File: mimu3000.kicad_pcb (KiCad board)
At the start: 2 copper layers, 54.4 x 26.2 mm, 14 parts, among them SW1 P_MISO, SW2 P_MOSI, U1 ATTINY13A-SSU, U2 H11F1M

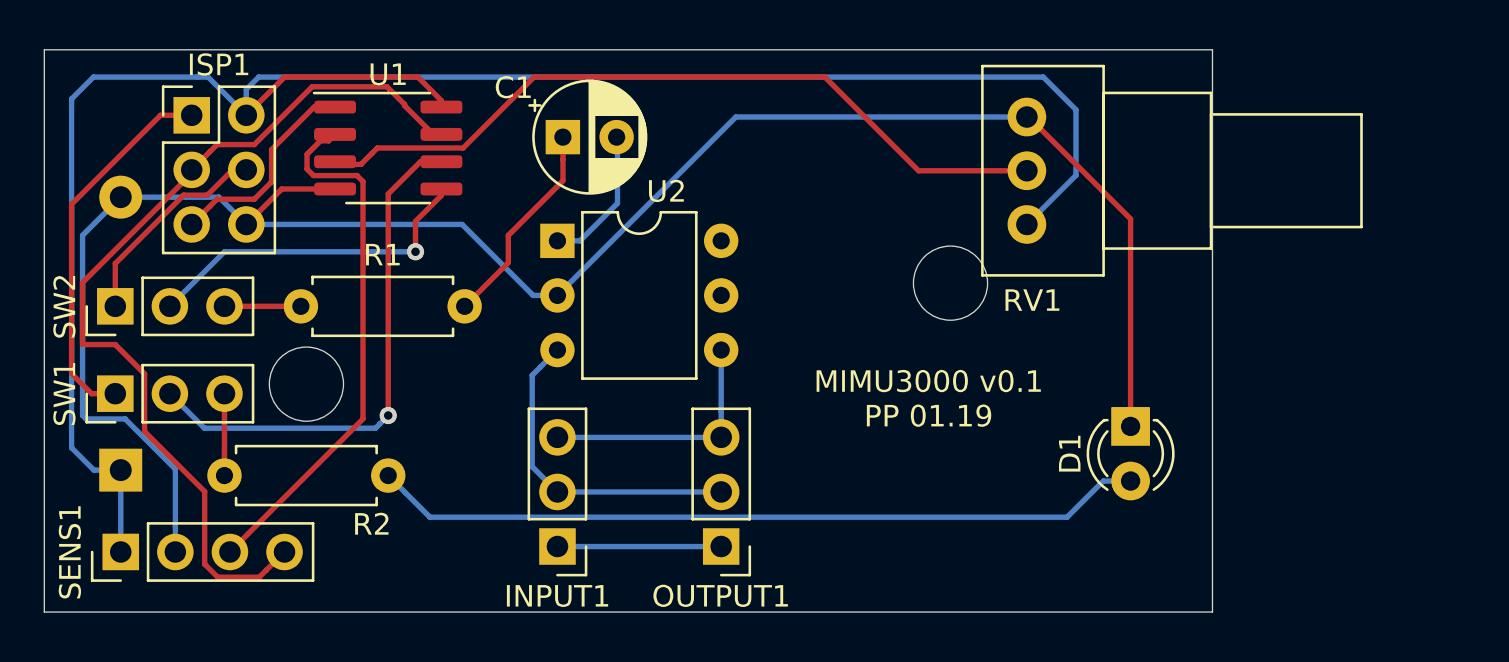
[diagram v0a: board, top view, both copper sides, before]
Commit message: Updated to using new low R_on optocoupler
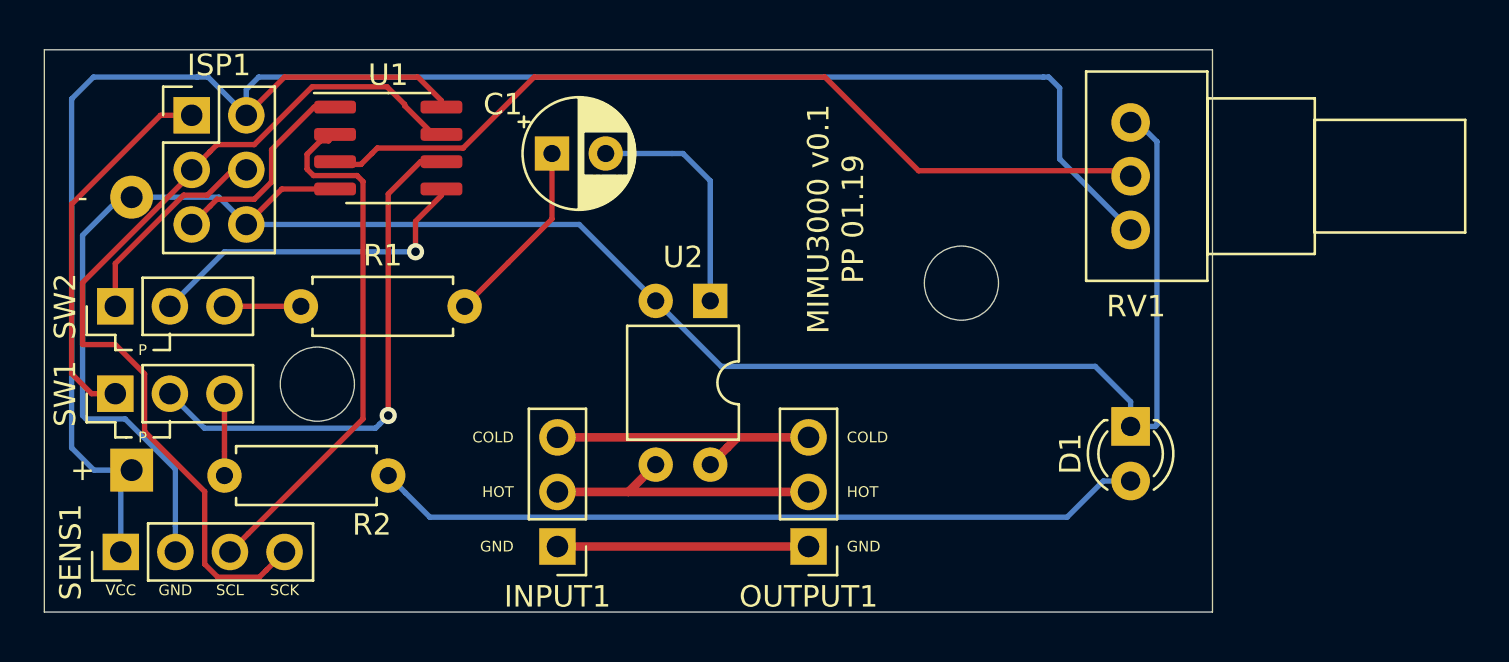
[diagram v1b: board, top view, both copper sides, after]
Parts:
- U2: value H11F1M -> AQY211EH; footprint Package_DIP:DIP-6_W7.62mm -> Package_DIP:DIP-4_W7.62mm
- moved U2 7.64 mm to (194.8, 112.3), turned to 270 degrees
- moved RV1 4.83 mm to (214.4, 109.0)
- moved OUTPUT1 4.06 mm to (199.4, 123.7)
- moved C1 0.92 mm to (187.5, 105.4)
- moved BT1 0.51 mm to (167.9, 120.1)
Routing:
- net Net-(RV1-Pad2): track 35.7 -> 40.7 mm
- net Net-(C1-Pad2): track 6.60 -> 11.0 mm
- net Net-(BT1-Pad2): track 88.9 -> 93.1 mm
- net Net-(INPUT1-Pad1): track 7.87 -> 11.7 mm
- net Net-(INPUT1-Pad3): track 11.7 -> 13.5 mm
- net Net-(INPUT1-Pad2): track 15.2 -> 13.5 mm
- net Net-(C1-Pad1): track 9.77 -> 8.80 mm
- net Net-(BT1-Pad1): track 89.6 -> 90.1 mm
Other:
- board text added: "+"
- board text added: "-"
- board text added: "COLD"
- board text added: "GND"
- board text added: "HOT"
- board text added: "P"
- board text added: "SCK"
- board text added: "SCL"
- board text added: "VCC"

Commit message: Fixed courtyard
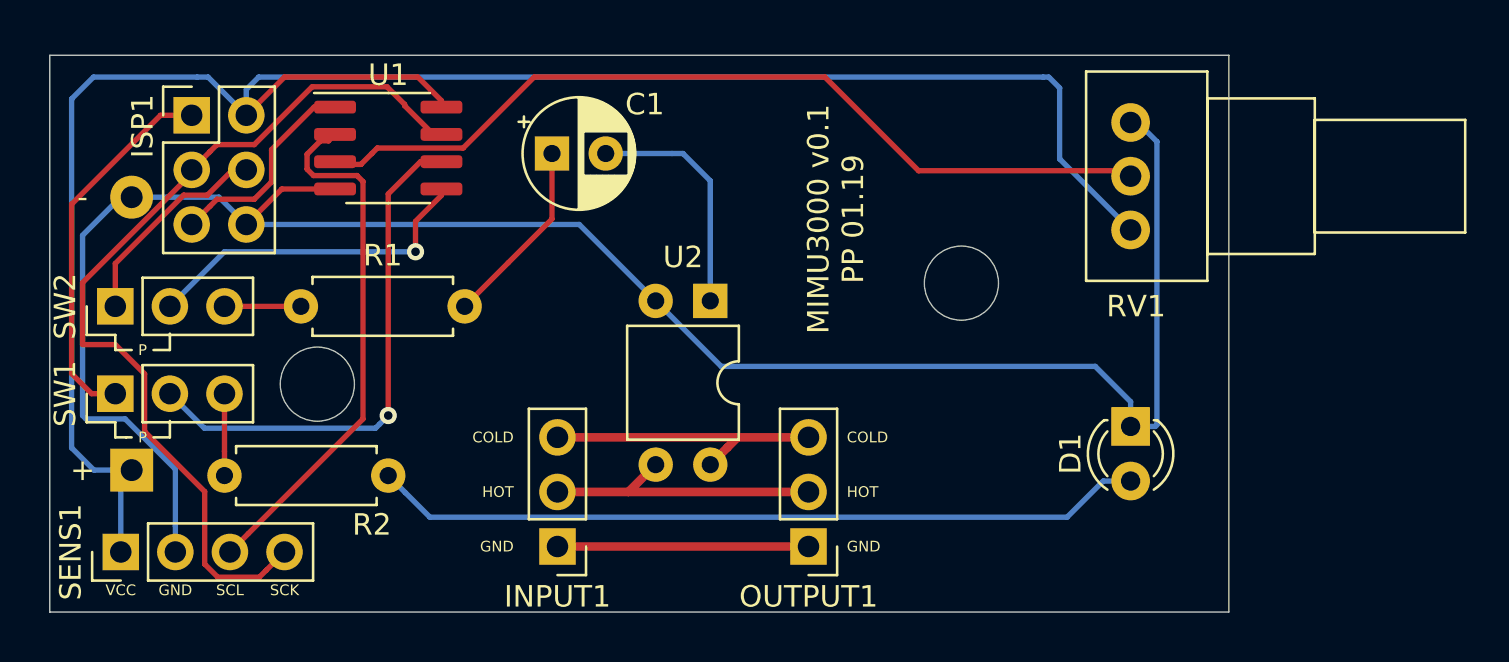
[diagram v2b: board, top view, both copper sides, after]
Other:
- board size 54.4 x 26.2 mm -> 54.9 x 25.9 mm
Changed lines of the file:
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@@
   (general
     (thickness 1.6)
-    (drawings 39)
+    (drawings 38)
     (tracks 138)
     (zones 0)
@@
     (descr "Through hole straight pin header, 2x03, 2.54mm pitch, double rows")
     (tags "Through hole pin header THT 2x03 2.54mm double row")
-    (fp_text reference ISP1 (at 1.27 -2.33) (layer F.SilkS)
+    (fp_text reference ISP1 (at -2.286 0.508 270) (layer F.SilkS)
       (effects (font (size 1 1) (thickness 0.15)))
     )
@@
     (descr "CP, Radial series, Radial, pin pitch=2.50mm, , diameter=5mm, Electrolytic Capacitor")
     (tags "CP Radial series Radial pin pitch 2.50mm  diameter 5mm Electrolytic Capacitor")
-    (fp_text reference C1 (at -2.286 -2.286) (layer F.SilkS)
+    (fp_text reference C1 (at 4.318 -2.286) (layer F.SilkS)
       (effects (font (size 1 1) (thickness 0.15)))
     )
@@
     )
   )
+  (gr_line (start 164.084 126.746) (end 164.084 100.838) (layer Edge.Cuts) (width 0.05))
+  (dimension 54.864 (width 0.15) (layer Dwgs.User)
+    (gr_text "54,864 mm" (at 191.516 138.099985) (layer Dwgs.User)
+      (effects (font (size 1 1) (thickness 0.15)))
+    )
+    (feature1 (pts (xy 218.948 126.746) (xy 218.948 137.386406)))
+    (feature2 (pts (xy 164.084 126.746) (xy 164.084 137.386406)))
+    (crossbar (pts (xy 164.084 136.799985) (xy 218.948 136.799985)))
+    (arrow1a (pts (xy 218.948 136.799985) (xy 217.821496 137.386406)))
+    (arrow1b (pts (xy 218.948 136.799985) (xy 217.821496 136.213564)))
+    (arrow2a (pts (xy 164.084 136.799985) (xy 165.210504 137.386406)))
+    (arrow2b (pts (xy 164.084 136.799985) (xy 165.210504 136.213564)))
+  )
   (gr_text GND (at 185.674 123.698) (layer F.SilkS)
     (effects (font (size 0.5 0.5) (thickness 0.1)) (justify right))
@@
   (gr_line (start 169.672 118.618) (end 169.672 117.856) (layer F.SilkS) (width 0.12))
   (gr_line (start 167.132 117.916) (end 167.132 118.618) (layer F.SilkS) (width 0.12))
-  (dimension 26.162 (width 0.15) (layer Dwgs.User)
-    (gr_text "26,162 mm" (at 159.99 113.665 90) (layer Dwgs.User)
-      (effects (font (size 1 1) (thickness 0.15)))
-    )
-    (feature1 (pts (xy 163.83 100.584) (xy 160.703579 100.584)))
-    (feature2 (pts (xy 163.83 126.746) (xy 160.703579 126.746)))
-    (crossbar (pts (xy 161.29 126.746) (xy 161.29 100.584)))
-    (arrow1a (pts (xy 161.29 100.584) (xy 161.876421 101.710504)))
-    (arrow1b (pts (xy 161.29 100.584) (xy 160.703579 101.710504)))
-    (arrow2a (pts (xy 161.29 126.746) (xy 161.876421 125.619496)))
-    (arrow2b (pts (xy 161.29 126.746) (xy 160.703579 125.619496)))
-  )
-  (dimension 54.356 (width 0.15) (layer Dwgs.User)
-    (gr_text "54,356 mm" (at 191.008 133.888) (layer Dwgs.User)
-      (effects (font (size 1 1) (thickness 0.15)))
-    )
-    (feature1 (pts (xy 218.186 126.746) (xy 218.186 133.174421)))
-    (feature2 (pts (xy 163.83 126.746) (xy 163.83 133.174421)))
-    (crossbar (pts (xy 163.83 132.588) (xy 218.186 132.588)))
-    (arrow1a (pts (xy 218.186 132.588) (xy 217.059496 133.174421)))
-    (arrow1b (pts (xy 218.186 132.588) (xy 217.059496 132.001579)))
-    (arrow2a (pts (xy 163.83 132.588) (xy 164.956504 133.174421)))
-    (arrow2b (pts (xy 163.83 132.588) (xy 164.956504 132.001579)))
+  (dimension 25.908 (width 0.15) (layer Dwgs.User)
+    (gr_text "25,908 mm" (at 160.244 113.792 90) (layer Dwgs.User)
+      (effects (font (size 1 1) (thickness 0.15)))
+    )
+    (feature1 (pts (xy 164.084 100.838) (xy 160.957579 100.838)))
+    (feature2 (pts (xy 164.084 126.746) (xy 160.957579 126.746)))
+    (crossbar (pts (xy 161.544 126.746) (xy 161.544 100.838)))
+    (arrow1a (pts (xy 161.544 100.838) (xy 162.130421 101.964504)))
+    (arrow1b (pts (xy 161.544 100.838) (xy 160.957579 101.964504)))
+    (arrow2a (pts (xy 161.544 126.746) (xy 162.130421 125.619496)))
+    (arrow2b (pts (xy 161.544 126.746) (xy 160.957579 125.619496)))
   )
   (gr_text "MIMU3000 v0.1\nPP 01.19" (at 200.66 108.458 90) (layer F.SilkS)
     (effects (font (size 1 1) (thickness 0.15)))
   )
-  (gr_line (start 163.83 100.584) (end 218.186 100.584) (layer Edge.Cuts) (width 0.05))
-  (gr_line (start 163.83 126.746) (end 163.83 100.584) (layer Edge.Cuts) (width 0.05))
-  (gr_line (start 218.186 126.746) (end 163.83 126.746) (layer Edge.Cuts) (width 0.05))
-  (gr_line (start 218.186 100.584) (end 218.186 126.746) (layer Edge.Cuts) (width 0.05))
-  (gr_line (start 163.83 126.746) (end 163.83 100.584) (layer B.CrtYd) (width 0.05))
-  (gr_line (start 218.186 126.746) (end 163.83 126.746) (layer B.CrtYd) (width 0.05))
-  (gr_line (start 218.186 100.584) (end 218.186 126.746) (layer B.CrtYd) (width 0.05))
-  (gr_line (start 163.83 100.584) (end 218.186 100.584) (layer B.CrtYd) (width 0.05))
-  (gr_line (start 218.186 100.584) (end 218.186 101.092) (layer F.CrtYd) (width 0.05))
-  (gr_line (start 163.83 100.584) (end 218.186 100.584) (layer F.CrtYd) (width 0.05))
-  (gr_line (start 163.83 126.746) (end 163.83 100.584) (layer F.CrtYd) (width 0.05))
-  (gr_line (start 218.186 126.746) (end 163.83 126.746) (layer F.CrtYd) (width 0.05))
-  (gr_line (start 218.186 101.092) (end 218.186 126.746) (layer F.CrtYd) (width 0.05))
+  (gr_line (start 164.084 100.838) (end 218.948 100.838) (layer Edge.Cuts) (width 0.05))
+  (gr_line (start 218.948 126.746) (end 164.084 126.746) (layer Edge.Cuts) (width 0.05))
+  (gr_line (start 218.948 100.838) (end 218.948 126.746) (layer Edge.Cuts) (width 0.05))
+  (gr_line (start 164.084 126.746) (end 164.084 100.838) (layer B.CrtYd) (width 0.05))
+  (gr_line (start 218.186 126.746) (end 164.084 126.746) (layer B.CrtYd) (width 0.05))
+  (gr_line (start 218.948 100.838) (end 218.948 126.746) (layer B.CrtYd) (width 0.05))
+  (gr_line (start 164.084 100.838) (end 218.948 100.838) (layer B.CrtYd) (width 0.05))
+  (gr_line (start 164.084 100.838) (end 218.948 100.838) (layer F.CrtYd) (width 0.05))
+  (gr_line (start 164.084 126.746) (end 164.084 100.838) (layer F.CrtYd) (width 0.05))
+  (gr_line (start 218.186 126.746) (end 164.084 126.746) (layer F.CrtYd) (width 0.05))
+  (gr_line (start 218.948 100.838) (end 218.948 126.746) (layer F.CrtYd) (width 0.05))
   (segment (start 174.879 107.061) (end 173.228 108.712) (width 0.25) (layer F.Cu) (net 1))
   (segment (start 177.357 107.061) (end 174.879 107.061) (width 0.25) (layer F.Cu) (net 1))
